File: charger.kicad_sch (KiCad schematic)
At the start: 14 parts, among them U2 LTC4121IUDTRPBF

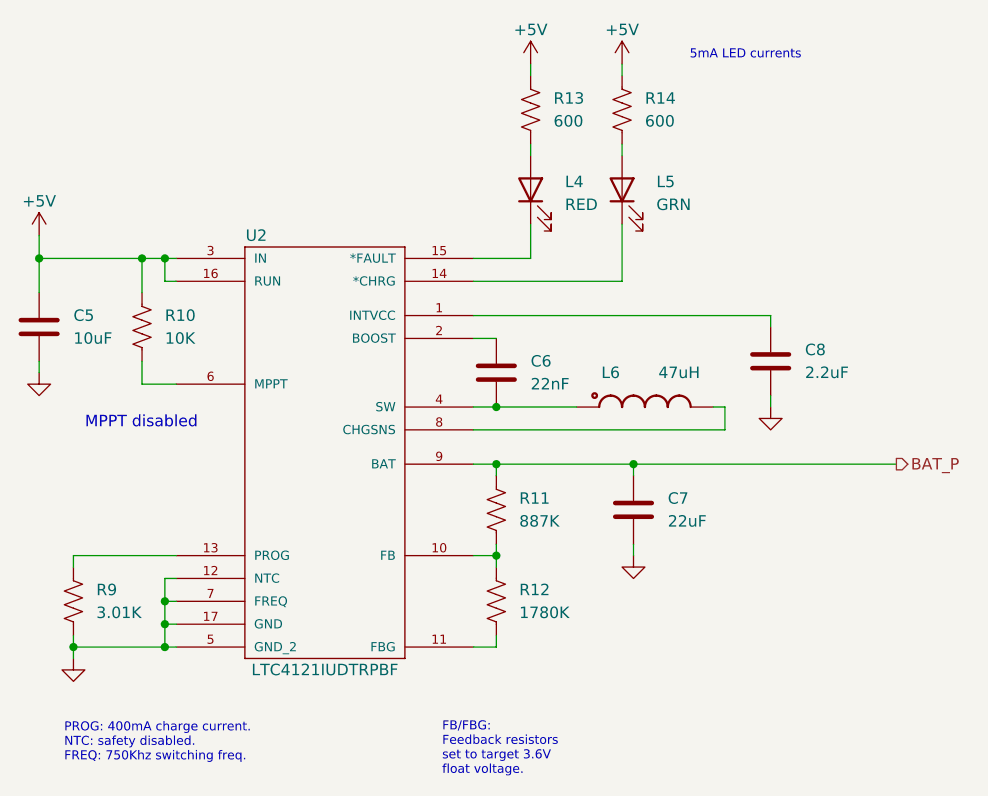
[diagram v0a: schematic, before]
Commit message: Rev 2, add ideal diode
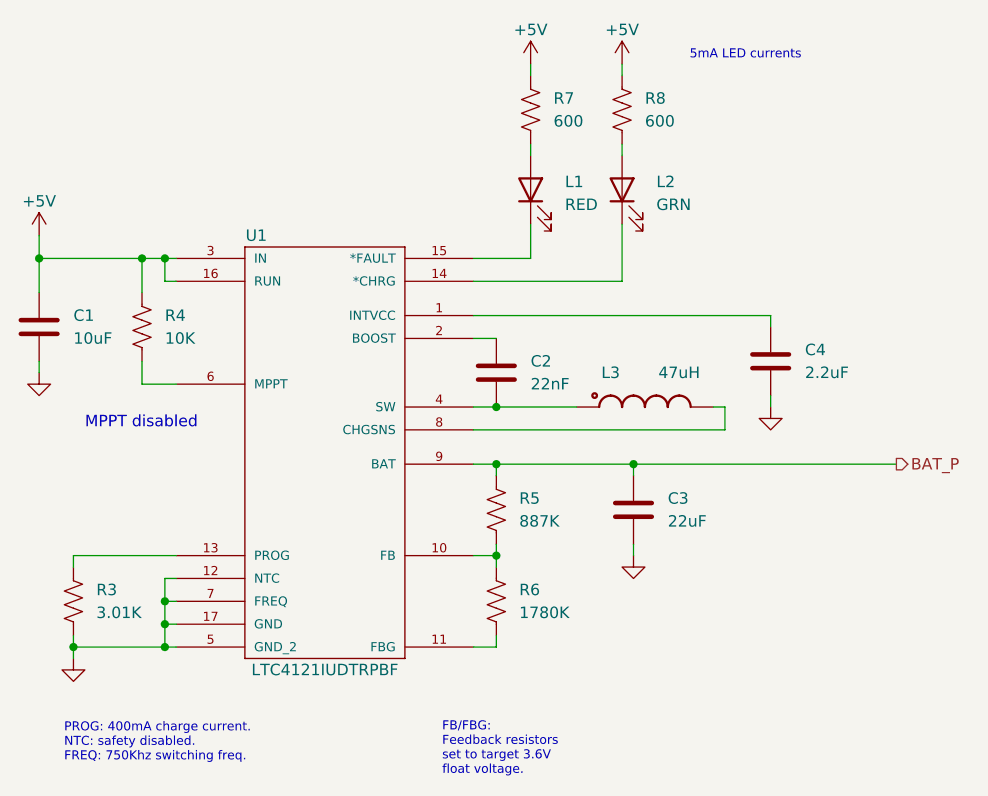
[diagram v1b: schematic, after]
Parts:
- renumbered C5 to C1, C6 to C2, C7 to C3, C8 to C4, L4 to L1, L5 to L2, L6 to L3, R9 to R3, R10 to R4, R11 to R5, R12 to R6, R13 to R7, R14 to R8, U2 to U1
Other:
- title: LTC4121 Charger Circuit -> 18650 Charger
